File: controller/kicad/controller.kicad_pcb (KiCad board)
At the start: 2 copper layers, 90 x 80 mm, 22 parts, among them J1 pcie_98, U1 ESD5344D, U10 ESD5344D, U11 WeAct_STM32H750_Module, U12 ESD5344D, U13 ESD5344D, U14 ESD5344D, U15 ESD5344D, U16 ESD5344D, U17 ESD5344D, U18 ESD5344D, U19 ESD5344D, U2 ESD5344D, U20 ESD5344D, U21 ESD5344D, U3 ESD5344D, U4 ESD5344D, U5 ESD5344D, U6 ESD5344D, U7 ESD5344D, U8 ESD5344D, U9 ESD5344D

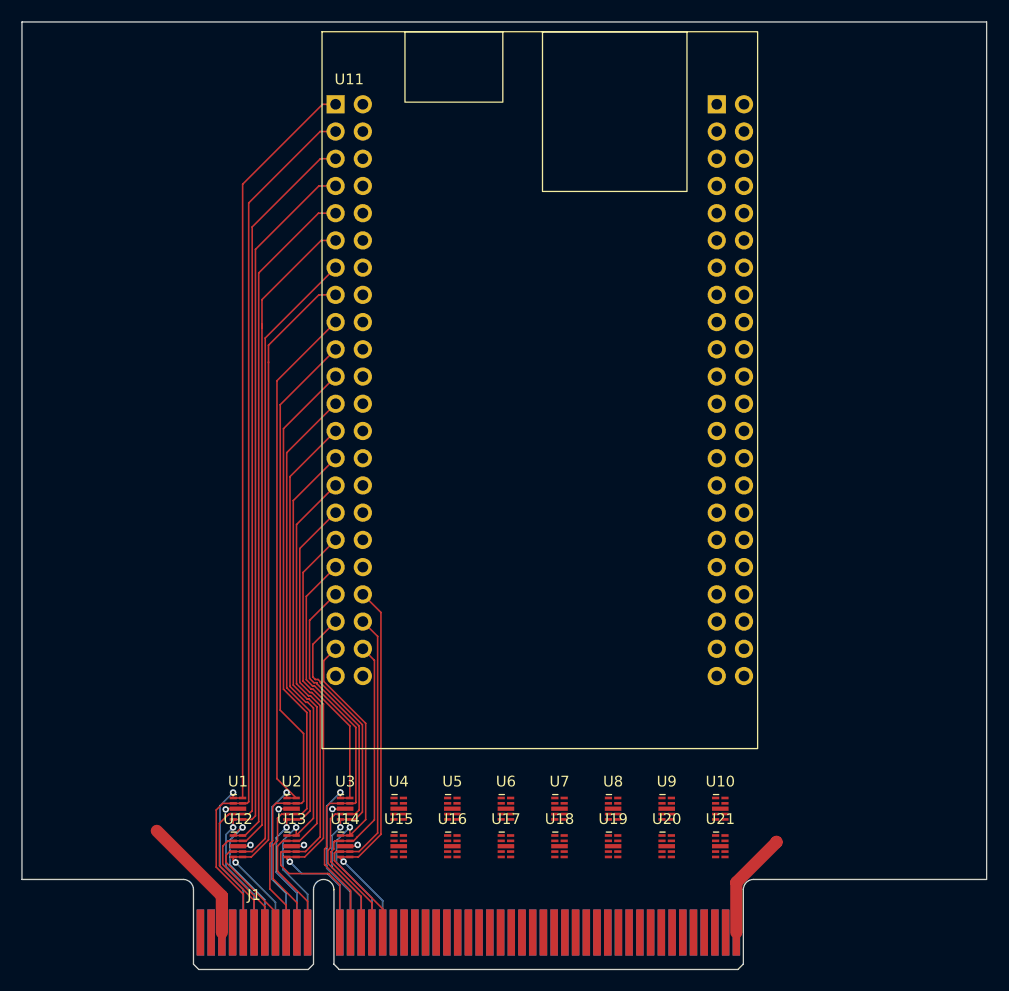
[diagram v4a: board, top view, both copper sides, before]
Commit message: More progress on routing the controller board.
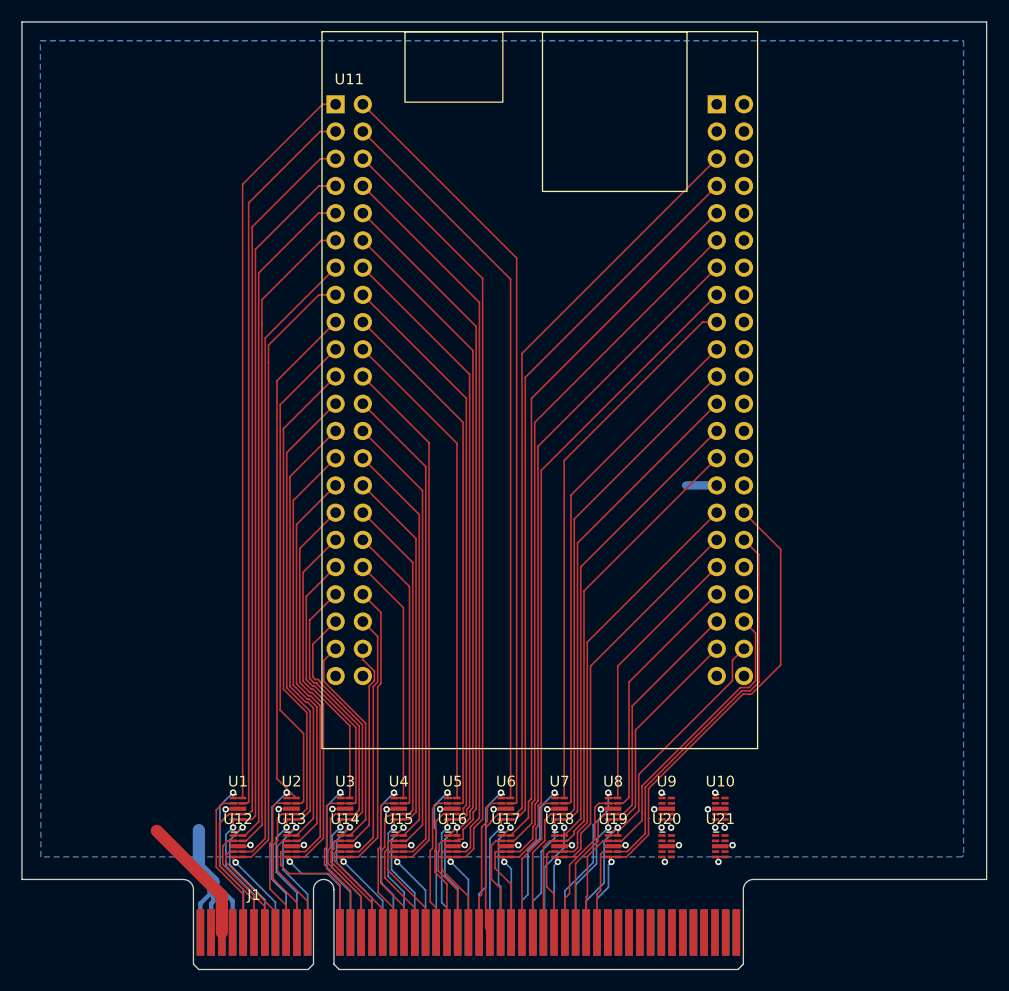
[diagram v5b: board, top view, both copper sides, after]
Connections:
- J1 pad A17: /A -> /PB4
- J1 pad A18: /A -> /PD3
- J1 pad A19: /A -> /PD1
- J1 pad A20: /A -> /PA12
- J1 pad A21: /A -> /PA10
- J1 pad A22: /A -> /PC6
- J1 pad A23: /A -> /PD14
- J1 pad A24: /A -> /PD8
- J1 pad A25: /A -> /PB14
- J1 pad A26: /A -> /PE14
- J1 pad A27: /A -> /PE12
- J1 pad A28: /A -> /PB2
- J1 pad A29: /A -> /PB0
- J1 pad A30: /A -> /PA4
- J1 pad A31: /A -> /PA2
- J1 pad A32: /A -> /PC0
- J1 pad A33: /A -> /PC13
- J1 pad A34: /A -> /PE2
- J1 pad A35: /A -> /PE3
- J1 pad A36: /A -> /PC3
- J1 pad A37: /A -> /PA1
- J1 pad A38: /A -> /PA7
- J1 pad A39: /A -> /PC5
- J1 pad A40: /A -> /PE9
- J1 pad A41: /A -> /PE11
- J1 pad A42: /A -> /PB11
- J1 pad B17: /B -> /PD7
- J1 pad B18: /B -> /PD5
- J1 pad B19: /B -> /PC12
- J1 pad B20: /B -> /PC10
- J1 pad B21: /B -> /PA8
- J1 pad B22: /B -> /PC8
- J1 pad B23: /B -> /PD12
- J1 pad B24: /B -> /PD10
- J1 pad B25: /B -> /PB12
- J1 pad B26: /B -> /PB10
- J1 pad B27: /B -> /PE10
- J1 pad B28: /B -> /PE8
- J1 pad B29: /B -> /PC4
- J1 pad B30: /B -> /PA6
- J1 pad B31: /B -> /PA0
- J1 pad B32: /B -> /PC2
- J1 pad B33: /B -> /PE6
- J1 pad B34: /B -> /PE4
- J1 pad B35: /B -> /PE5
- J1 pad B36: /B -> /PC1
- J1 pad B37: /B -> /PA3
- J1 pad B38: /B -> /PA5
- J1 pad B39: /B -> /PB1
- J1 pad B40: /B -> /PE7
- J1 pad B41: /B -> /PE13
- J1 pad B42: /B -> /PE15
- U10 pad 1: /X -> /PE11
- U10 pad 2: /X -> /PE13
- U10 pad 3: unconnected-(U10-Pad3) -> GND
- U10 pad 4: /X -> /PE15
- U10 pad 5: /X -> /PB11
- U15 pad 1: /X -> /PD1
- U15 pad 2: /X -> /PC12
- U15 pad 3: unconnected-(U15-Pad3) -> GND
- U15 pad 4: /X -> /PC10
- U15 pad 5: /X -> /PA12
- U16 pad 1: /X -> /PD14
- U16 pad 2: /X -> /PD12
- U16 pad 3: unconnected-(U16-Pad3) -> GND
- U16 pad 4: /X -> /PD10
- U16 pad 5: /X -> /PD8
- U17 pad 1: /X -> /PE12
- U17 pad 2: /X -> /PE10
- U17 pad 3: unconnected-(U17-Pad3) -> GND
- U17 pad 4: /X -> /PE8
- U17 pad 5: /X -> /PB2
- U18 pad 1: /X -> /PA2
- U18 pad 2: /X -> /PA0
- U18 pad 3: unconnected-(U18-Pad3) -> GND
- U18 pad 4: /X -> /PC2
- U18 pad 5: /X -> /PC0
- U19 pad 1: /X -> /PE3
- U19 pad 2: /X -> /PE5
- U19 pad 3: unconnected-(U19-Pad3) -> GND
- U19 pad 4: /X -> /PC1
- U19 pad 5: /X -> /PC3
- U20 pad 1: /X -> /PC5
- U20 pad 2: /X -> /PB1
- U20 pad 3: unconnected-(U20-Pad3) -> GND
- U20 pad 4: /X -> /PE7
- U20 pad 5: /X -> /PE9
- U21 pad 1: /X -> unconnected-(U21-Pad1)
- U21 pad 2: /X -> unconnected-(U21-Pad2)
- U21 pad 3: unconnected-(U21-Pad3) -> GND
- U21 pad 4: /X -> unconnected-(U21-Pad4)
- U21 pad 5: /X -> unconnected-(U21-Pad5)
- U4 pad 1: /X -> /PB4
- U4 pad 2: /X -> /PD7
- U4 pad 3: unconnected-(U4-Pad3) -> GND
- U4 pad 4: /X -> /PD5
- U4 pad 5: /X -> /PD3
- U5 pad 1: /X -> /PA10
- U5 pad 2: /X -> /PA8
- U5 pad 3: unconnected-(U5-Pad3) -> GND
- U5 pad 4: /X -> /PC8
- U5 pad 5: /X -> /PC6
- U6 pad 1: /X -> /PB14
- U6 pad 2: /X -> /PB12
- U6 pad 3: unconnected-(U6-Pad3) -> GND
- U6 pad 4: /X -> /PB10
- U6 pad 5: /X -> /PE14
- U7 pad 1: /X -> /PB0
- U7 pad 2: /X -> /PC4
- U7 pad 3: unconnected-(U7-Pad3) -> GND
- U7 pad 4: /X -> /PA6
- U7 pad 5: /X -> /PA4
- U8 pad 1: /X -> /PC13
- U8 pad 2: /X -> /PE6
- U8 pad 3: unconnected-(U8-Pad3) -> GND
- U8 pad 4: /X -> /PE4
- U8 pad 5: /X -> /PE2
- U9 pad 1: /X -> /PA1
- U9 pad 2: /X -> /PA3
- U9 pad 3: unconnected-(U9-Pad3) -> GND
- U9 pad 4: /X -> /PA5
- U9 pad 5: /X -> /PA7
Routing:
- net /PB12: track 0.00 -> 86.0 mm
- net /PB14: track 0.00 -> 83.2 mm, vias 0 -> 1
- net /PB10: track 0.00 -> 82.2 mm
- net /PD8: track 0.00 -> 80.0 mm, vias 0 -> 1
- net /PE14: track 0.00 -> 79.2 mm, vias 0 -> 1
- net /PE12: track 0.00 -> 78.4 mm, vias 0 -> 1
- net /PD10: track 0.00 -> 77.9 mm
- net /PD12: track 0.00 -> 74.7 mm
- net /PE10: track 0.00 -> 74.6 mm
- net /PD14: track 0.00 -> 73.2 mm, vias 0 -> 1
- net /PE8: track 0.00 -> 72.5 mm
- net /PB2: track 0.00 -> 69.2 mm, vias 0 -> 1
- net /PC6: track 0.00 -> 68.2 mm, vias 0 -> 1
- net /PB0: track 0.00 -> 66.7 mm, vias 0 -> 1
- net /PC8: track 0.00 -> 66.2 mm
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- added copper zone on B.Cu, net GND

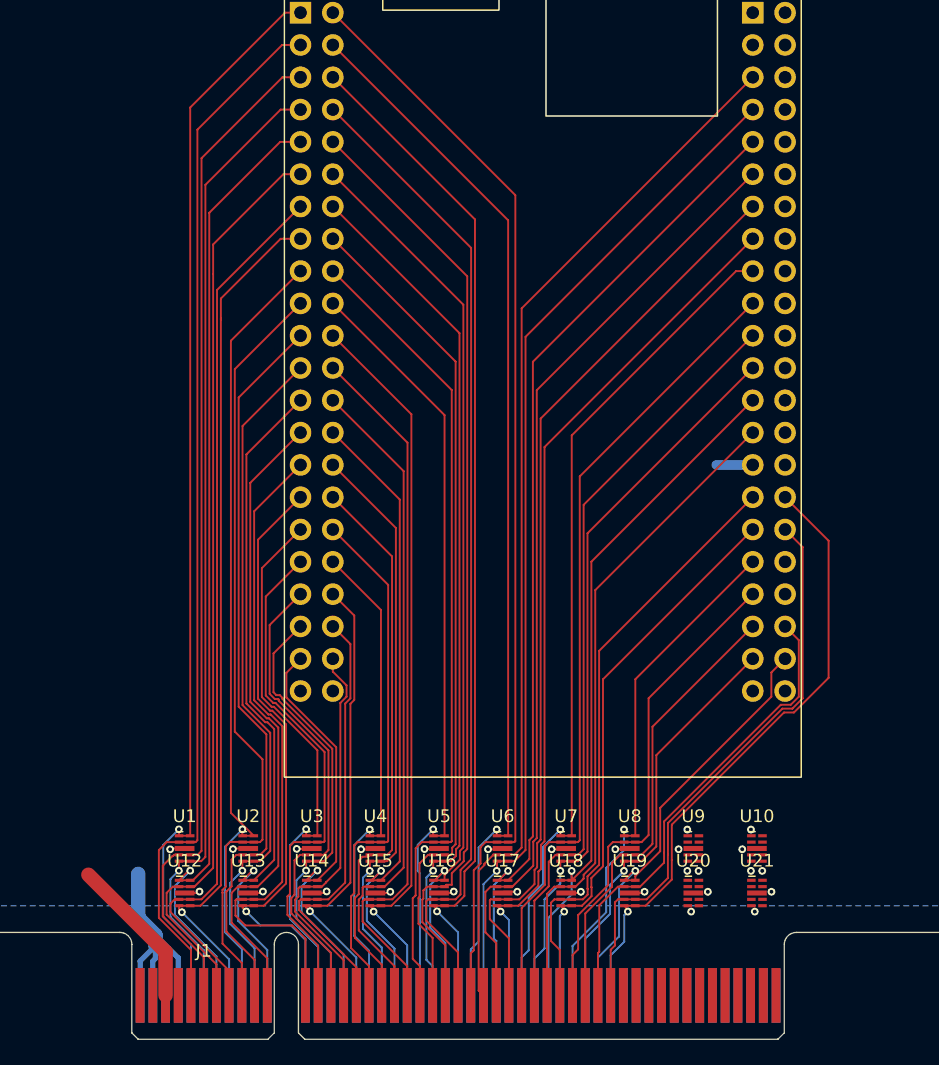
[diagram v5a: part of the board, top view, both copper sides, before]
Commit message: First pass of routing all the MCU signals. Needs cleanup.
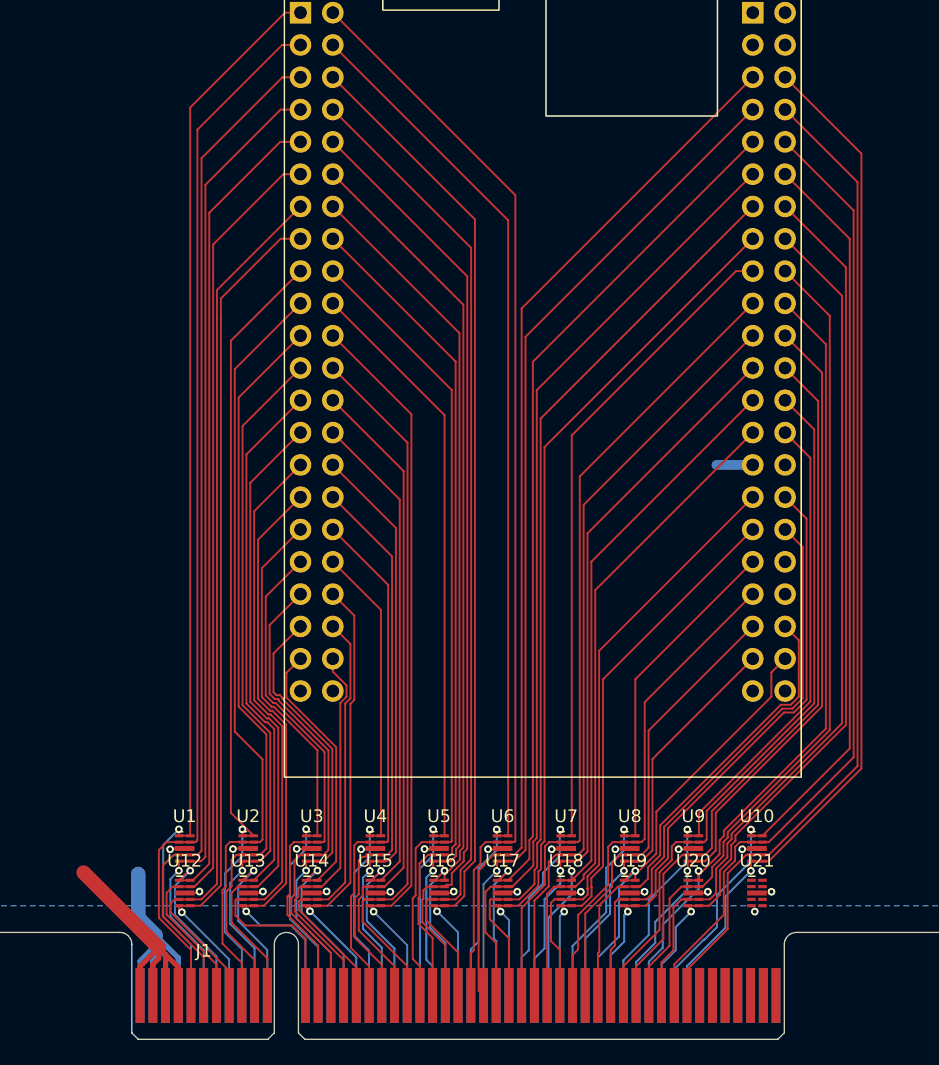
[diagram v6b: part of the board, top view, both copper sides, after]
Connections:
- J1 pad A43: /A -> unconnected-(J1-Pin_a43-PadA43)
- J1 pad A44: /A -> unconnected-(J1-Pin_a44-PadA44)
- J1 pad A45: /A -> unconnected-(J1-Pin_a45-PadA45)
- J1 pad A46: /A -> unconnected-(J1-Pin_a46-PadA46)
- J1 pad A47: /A -> unconnected-(J1-Pin_a47-PadA47)
- J1 pad B43: /B -> unconnected-(J1-Pin_b43-PadB43)
- J1 pad B44: /B -> unconnected-(J1-Pin_b44-PadB44)
- J1 pad B45: /B -> unconnected-(J1-Pin_b45-PadB45)
- J1 pad B46: /B -> unconnected-(J1-Pin_46-PadB46)
- J1 pad B47: /B -> unconnected-(J1-Pin_b47-PadB47)
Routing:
- net /PB11: track 0.00 -> 81.2 mm
- net /PE15: track 0.00 -> 79.5 mm
- net /PE13: track 0.00 -> 76.5 mm
- net /PE11: track 0.00 -> 73.9 mm
- net /PE9: track 0.00 -> 71.2 mm
- net /PE7: track 0.00 -> 68.5 mm
- net /PB1: track 0.00 -> 65.3 mm
- net /PC5: track 0.00 -> 63.9 mm
- net /PA7: track 0.00 -> 59.9 mm
- net /PA5: track 0.00 -> 57.9 mm
- net /PA3: track 0.00 -> 55.3 mm
- net /PA1: track 0.00 -> 52.7 mm
- net +5V: track 12.0 -> 25.0 mm
- net GND: track 46.0 -> 49.6 mm
- net /PC3: track 49.4 -> 47.9 mm

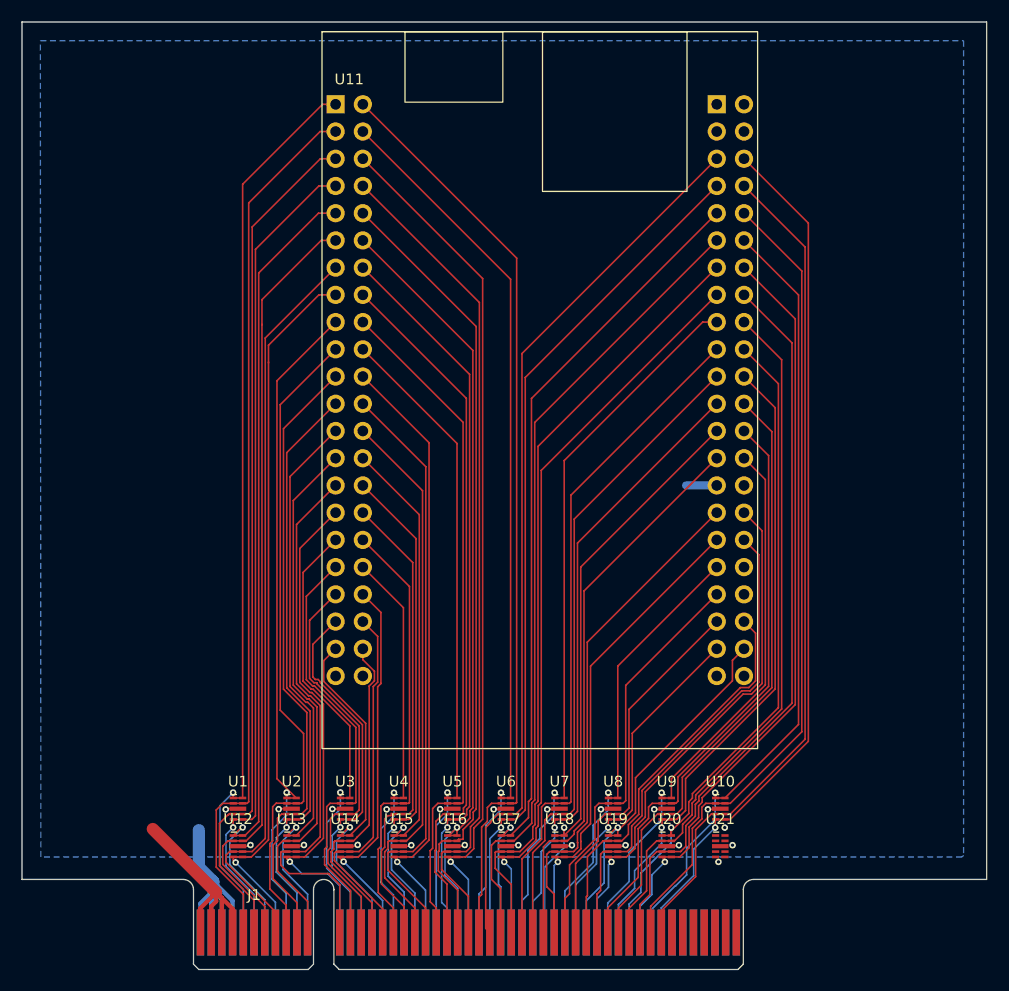
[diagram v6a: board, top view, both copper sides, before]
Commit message: Controller board passes ERC and DRC. Needs more cleanup.
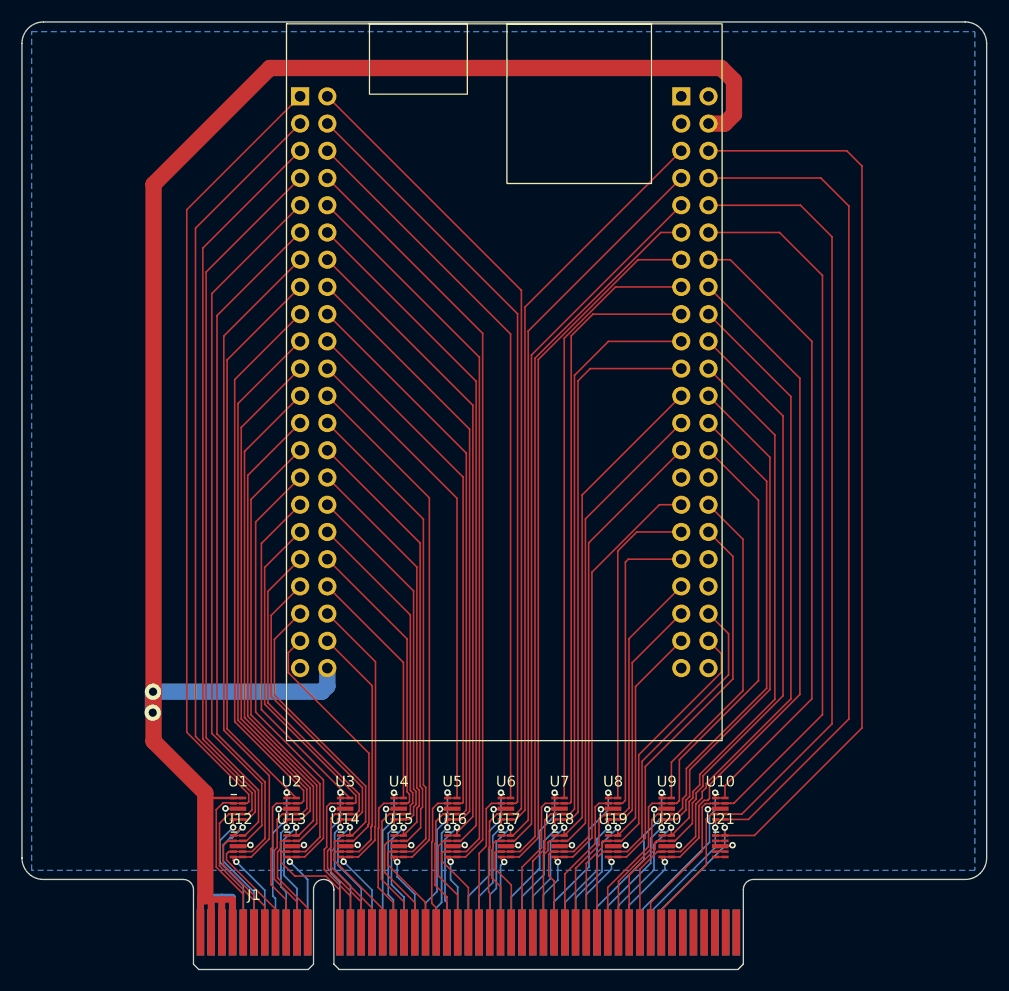
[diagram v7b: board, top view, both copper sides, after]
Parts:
- moved U11 3.39 mm to (86.8, 5.21)
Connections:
- J1 pad A11: /PD0 -> /PD4
- J1 pad A13: /PB3 -> /PB7
- J1 pad A15: /PE1 -> /PB8
- J1 pad A17: /PB4 -> /PD5
- J1 pad A19: /PD1 -> /PC10
- J1 pad A21: /PA10 -> /PC8
- J1 pad A23: /PD14 -> /PD10
- J1 pad A25: /PB14 -> /PB10
- J1 pad A27: /PE12 -> /PE8
- J1 pad A29: /PB0 -> /PA6
- J1 pad A31: /PA2 -> /PC2
- J1 pad A33: /PC13 -> /PE4
- J1 pad A35: /PE3 -> /PC1
- J1 pad A37: /PA1 -> /PA5
- J1 pad A39: /PC5 -> /PE7
- J1 pad A41: /PE11 -> /PE15
- J1 pad A48: /VIN- -> unconnected-(J1-Pin_a48-PadA48)
- J1 pad A49: /VIN- -> unconnected-(J1-Pin_a49-PadA49)
- J1 pad A5: /PB13 -> /PD9
- J1 pad A7: /PD13 -> /PC7
- J1 pad A9: /PA9 -> /PA15
- J1 pad B1: +5V -> /+5V
- J1 pad B10: /PA15 -> /PA11
- J1 pad B11: /PD2 -> /PD0
- J1 pad B12: /PD4 -> /PD2
- J1 pad B13: /PB5 -> /PB3
- J1 pad B14: /PB7 -> /PB5
- J1 pad B15: /PE0 -> /PE1
- J1 pad B16: /PB8 -> /PE0
- J1 pad B17: /PD7 -> /PB4
- J1 pad B18: /PD5 -> /PD7
- J1 pad B19: /PC12 -> /PD1
- J1 pad B2: +5V -> /+5V
- J1 pad B20: /PC10 -> /PC12
- J1 pad B21: /PA8 -> /PA10
- J1 pad B22: /PC8 -> /PA8
- J1 pad B23: /PD12 -> /PD14
- J1 pad B24: /PD10 -> /PD12
- J1 pad B25: /PB12 -> /PB14
- J1 pad B26: /PB10 -> /PB12
- J1 pad B27: /PE10 -> /PE12
- J1 pad B28: /PE8 -> /PE10
- J1 pad B29: /PC4 -> /PB0
- J1 pad B3: +5V -> /+5V
- J1 pad B30: /PA6 -> /PC4
- J1 pad B31: /PA0 -> /PA2
- J1 pad B32: /PC2 -> /PA0
- J1 pad B33: /PE6 -> /PC13
- J1 pad B34: /PE4 -> /PE6
- J1 pad B35: /PE5 -> /PE3
- J1 pad B36: /PC1 -> /PE5
- J1 pad B37: /PA3 -> /PA1
- J1 pad B38: /PA5 -> /PA3
- J1 pad B39: /PB1 -> /PC5
- J1 pad B4: +5V -> /+5V
- J1 pad B40: /PE7 -> /PB1
- J1 pad B41: /PE13 -> /PE11
- J1 pad B42: /PE15 -> /PE13
- J1 pad B48: /VIN+ -> unconnected-(J1-Pin_b48-PadB48)
- J1 pad B49: /VIN+ -> unconnected-(J1-Pin_b49-PadB49)
- J1 pad B5: /PB15 -> /PB13
- J1 pad B6: /PD9 -> /PB15
- J1 pad B7: /PD15 -> /PD13
- J1 pad B8: /PC7 -> /PD15
- J1 pad B9: /PA11 -> /PA9
- U1 pad 1: /PB13 -> /+5V
- U1 pad 2: /PB15 -> /PB13
- U1 pad 4: /PD9 -> /PB15
- U1 pad 5: /PD11 -> /PD9
- U10 pad 1: /PE11 -> /PE9
- U10 pad 2: /PE13 -> /PE11
- U10 pad 4: /PE15 -> /PE13
- U10 pad 5: /PB11 -> /PE15
- U11 pad 44: +5V -> /+5V
- U11 pad 47: +3V3 -> unconnected-(U11B-+3V3-Pad47)
- U11 pad 48: +5V -> /+5V
- U11 pad 88: +3V3 -> unconnected-(U11B-+3V3-Pad88)
- U12 pad 1: /PD13 -> /PD11
- U12 pad 2: /PD15 -> /PD13
- U12 pad 4: /PC7 -> /PD15
- U12 pad 5: /PC9 -> /PC7
- U13 pad 1: /PD0 -> /PC11
- U13 pad 2: /PD2 -> /PD0
- U13 pad 4: /PD4 -> /PD2
- U13 pad 5: /PD6 -> /PD4
- U14 pad 1: /PE1 -> /PB9
- U14 pad 2: /PE0 -> /PE1
- U14 pad 4: /PB8 -> /PE0
- U14 pad 5: /PB6 -> /PB8
- U15 pad 1: /PD1 -> /PD3
- U15 pad 2: /PC12 -> /PD1
- U15 pad 4: /PC10 -> /PC12
- U15 pad 5: /PA12 -> /PC10
- U16 pad 1: /PD14 -> /PC6
- U16 pad 2: /PD12 -> /PD14
- U16 pad 4: /PD10 -> /PD12
- U16 pad 5: /PD8 -> /PD10
- U17 pad 1: /PE12 -> /PE14
- U17 pad 2: /PE10 -> /PE12
- U17 pad 4: /PE8 -> /PE10
- U17 pad 5: /PB2 -> /PE8
- U18 pad 1: /PA2 -> /PA4
- U18 pad 2: /PA0 -> /PA2
- U18 pad 4: /PC2 -> /PA0
- U18 pad 5: /PC0 -> /PC2
- U19 pad 1: /PE3 -> /PE2
- U19 pad 2: /PE5 -> /PE3
- U19 pad 4: /PC1 -> /PE5
- U19 pad 5: /PC3 -> /PC1
- U2 pad 1: /PA9 -> /PC9
- U2 pad 2: /PA11 -> /PA9
- U2 pad 4: /PA15 -> /PA11
- U2 pad 5: /PC11 -> /PA15
- U20 pad 1: /PC5 -> /PA7
- U20 pad 2: /PB1 -> /PC5
- U20 pad 4: /PE7 -> /PB1
- U20 pad 5: /PE9 -> /PE7
- U21 pad 1: unconnected-(U21-D1-Pad1) -> /PB11
- U3 pad 1: /PB3 -> /PD6
- U3 pad 2: /PB5 -> /PB3
- U3 pad 4: /PB7 -> /PB5
- U3 pad 5: /PB9 -> /PB7
- U4 pad 1: /PB4 -> /PB6
- U4 pad 2: /PD7 -> /PB4
- U4 pad 4: /PD5 -> /PD7
- U4 pad 5: /PD3 -> /PD5
- U5 pad 1: /PA10 -> /PA12
- U5 pad 2: /PA8 -> /PA10
- U5 pad 4: /PC8 -> /PA8
- U5 pad 5: /PC6 -> /PC8
- U6 pad 1: /PB14 -> /PD8
- U6 pad 2: /PB12 -> /PB14
- U6 pad 4: /PB10 -> /PB12
- U6 pad 5: /PE14 -> /PB10
- U7 pad 1: /PB0 -> /PB2
- U7 pad 2: /PC4 -> /PB0
- U7 pad 4: /PA6 -> /PC4
- U7 pad 5: /PA4 -> /PA6
- U8 pad 1: /PC13 -> /PC0
- U8 pad 2: /PE6 -> /PC13
- U8 pad 4: /PE4 -> /PE6
- U8 pad 5: /PE2 -> /PE4
- U9 pad 1: /PA1 -> /PC3
- U9 pad 2: /PA3 -> /PA1
- U9 pad 4: /PA5 -> /PA3
- U9 pad 5: /PA7 -> /PA5
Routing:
- net /+5V: track 0.00 -> 172.4 mm, vias 0 -> 2
- net +5V: track 25.0 -> 0.00 mm
- net /PB11: track 81.2 -> 98.1 mm
- net /PE15: track 79.5 -> 91.4 mm, vias 0 -> 1
- net /PE13: track 76.5 -> 85.9 mm
- net /PE11: track 73.9 -> 81.8 mm, vias 1 -> 0
- net GND: track 49.6 -> 43.3 mm
- net /PD2: track 50.5 -> 56.3 mm
- net /PE9: track 71.2 -> 76.1 mm
- net /PD11: track 76.9 -> 81.6 mm
- net /PA6: track 60.0 -> 64.6 mm, vias 0 -> 1
- net /PC11: track 55.0 -> 59.0 mm
- net /PB9: track 35.1 -> 38.8 mm
- net /PC6: track 68.2 -> 71.9 mm
- net /PD3: track 46.2 -> 49.9 mm
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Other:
- outline, holes or cut-outs redrawn
